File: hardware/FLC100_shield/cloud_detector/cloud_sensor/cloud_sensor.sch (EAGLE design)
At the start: 12 parts, among them IC1 MLX90614, Q1 2N7000, X1 SHIELD, X2 SENSOR

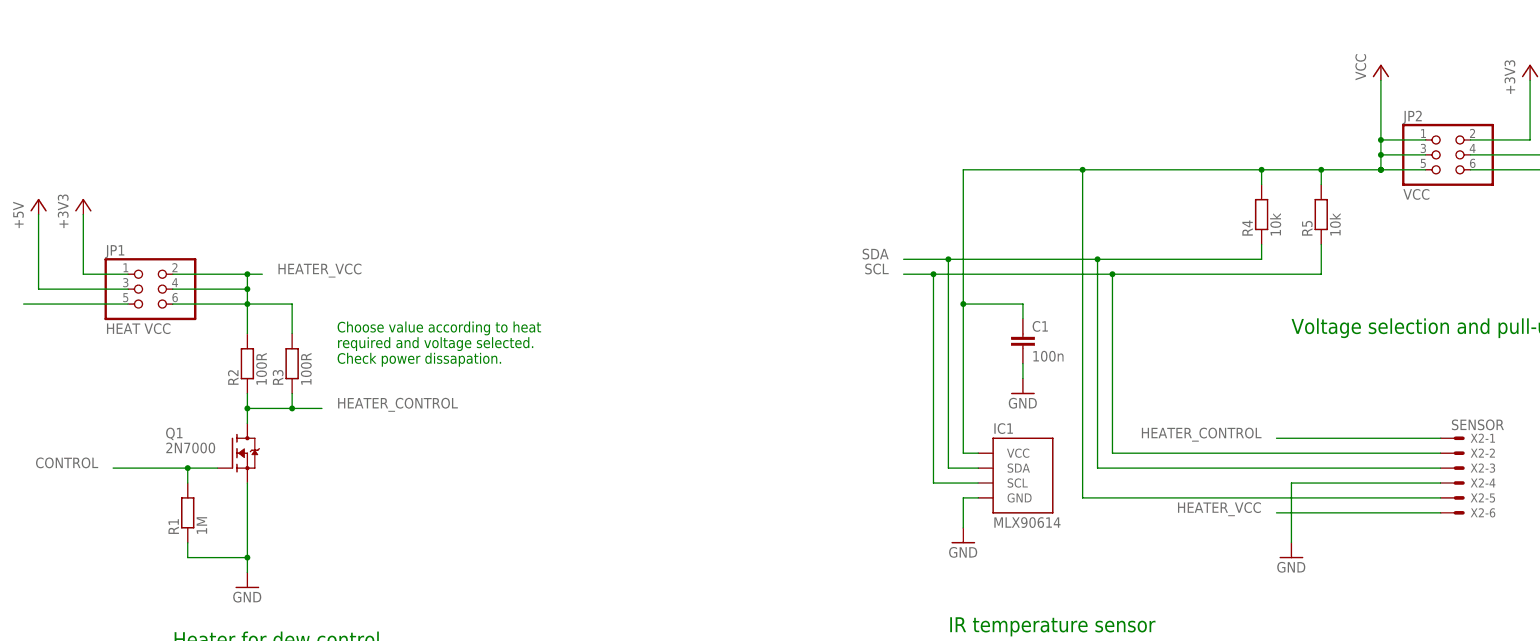
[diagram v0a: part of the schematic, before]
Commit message: Adding additional decoupling capacitor.
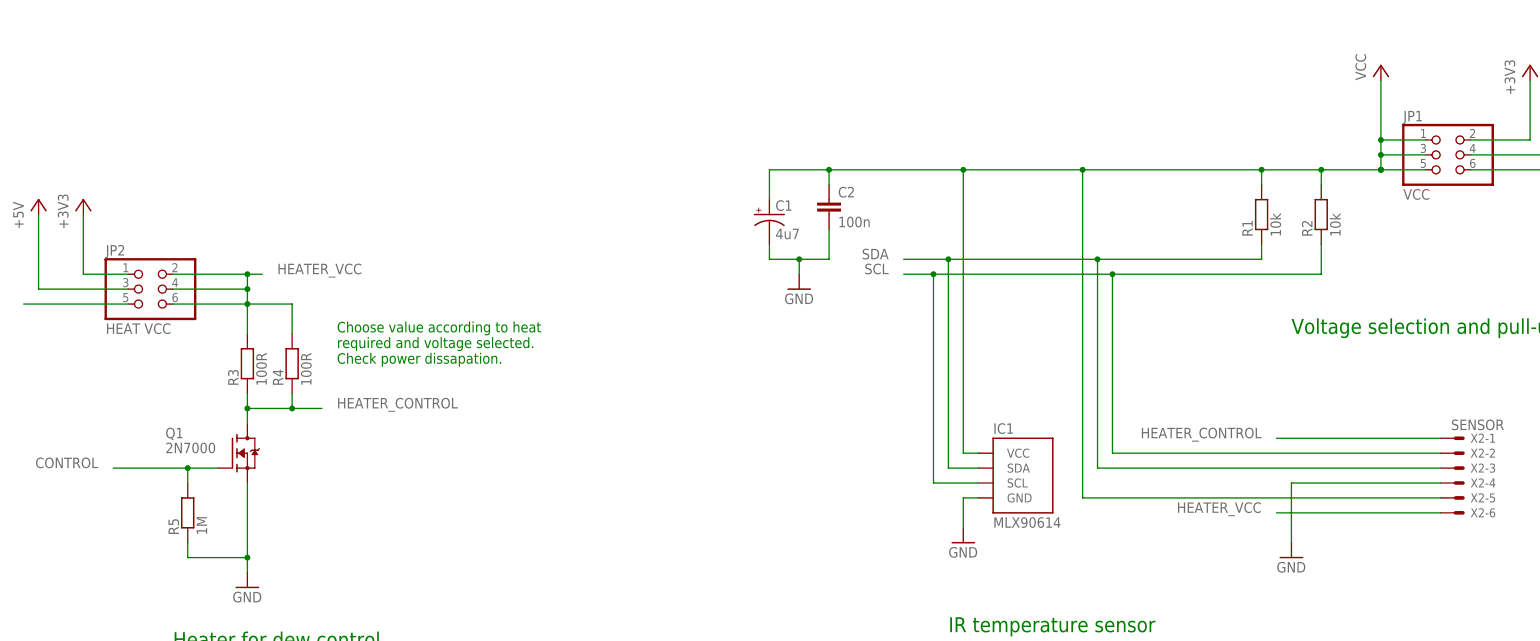
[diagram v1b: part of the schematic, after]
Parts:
- added C2: 100n, SparkFun:CAPPTH
- C1: value 100n -> 4u7; device SparkFun:CAPPTH -> SteveMarple:CAP_POLPTH2
- JP1: value HEAT VCC -> VCC
- JP2: value VCC -> HEAT VCC
- R1: value 1M -> 10k
- R2: value 100R -> 10k
- R4: value 10k -> 100R
- R5: value 10k -> 1M
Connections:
- net +3V3: now also JP1.2, JP2.1; no longer JP1.1, JP2.2
- net +5V: now also JP1.4, JP2.3; no longer JP1.3, JP2.4
- net CONTROL: now also JP1.6, R5.2; no longer JP2.6, R1.2
- net GND: now also C1.-, C2.2, R5.1; no longer C1.2, R1.1
- net HEATER_CONTROL: now also R4.1; no longer R2.1
- net HEATER_VCC: now also JP2.2, JP2.4, JP2.6, R4.2; no longer JP1.2, JP1.4, JP1.6, R2.2
- net SCL: now also R2.1; no longer R5.1
- net SDA: now also R1.1; no longer R4.1
- net VCC: now also C1.+, C2.1, JP1.1, JP1.3, JP1.5, R1.2, R2.2; no longer C1.1, JP2.1, JP2.3, JP2.5, R4.2, R5.2
- net VIN: now also JP2.5; no longer JP1.5
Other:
- moved on the sheet: JP1, JP2, R1, R2, R3, R4, R5
